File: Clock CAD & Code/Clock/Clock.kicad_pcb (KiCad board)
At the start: 2 copper layers, 140 x 90 mm, 64 parts, among them J1 Power_inlet_vertical, J2 Conn_01x06, SW1 RotaryEncoder_Switch, SW2 Omron_B3F_SPST, U1 L7805, U2 ATmega328-PU, U4 DS1307_DIP-8, U5 MAX7219, U6 MAX7219, Y1 Crystal 16MHZ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

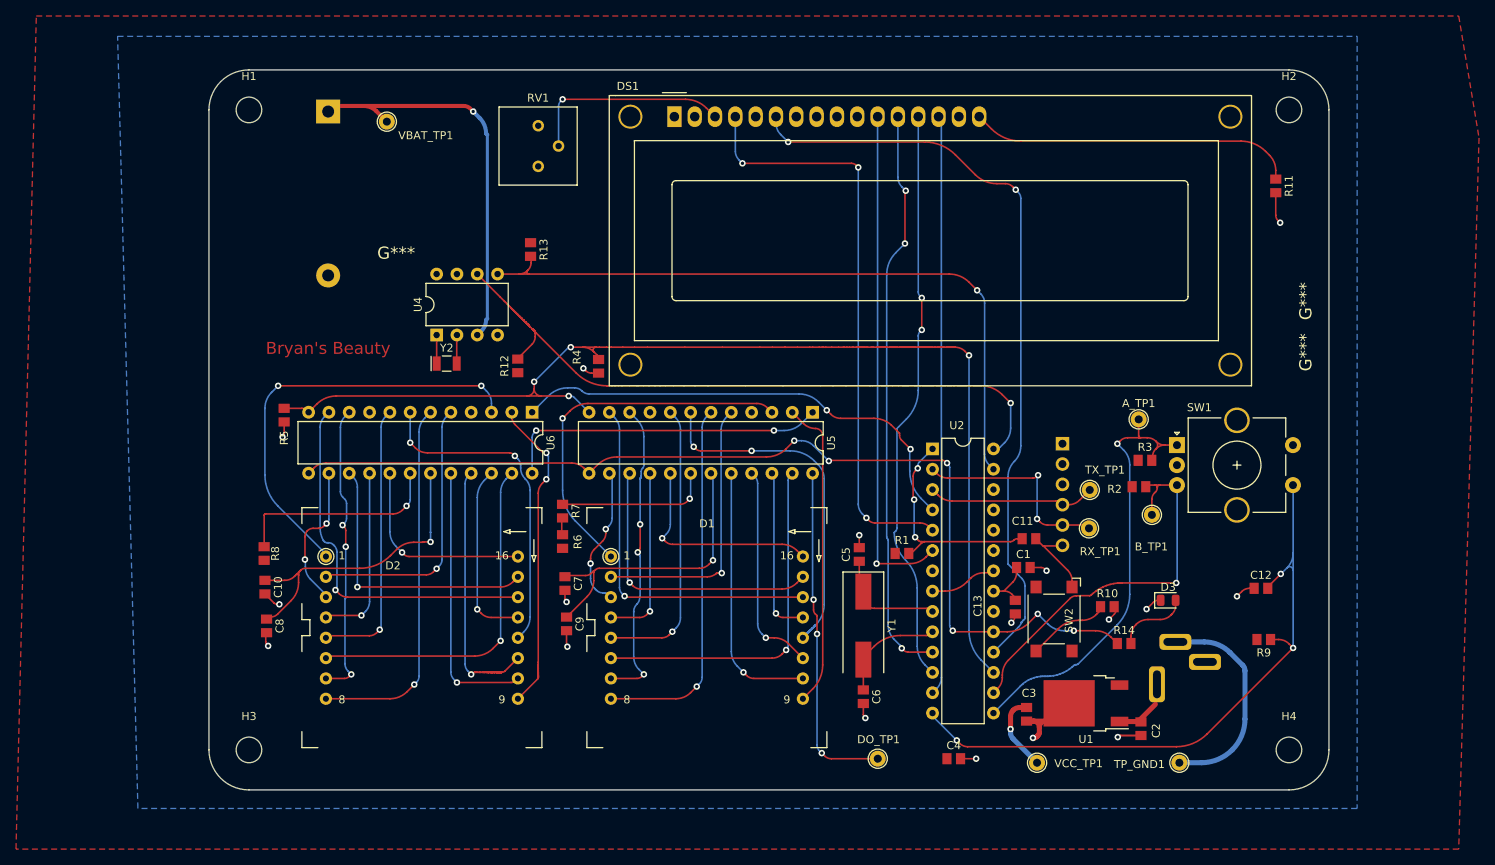
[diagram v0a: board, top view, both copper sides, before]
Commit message: Fixed DRC and ERC
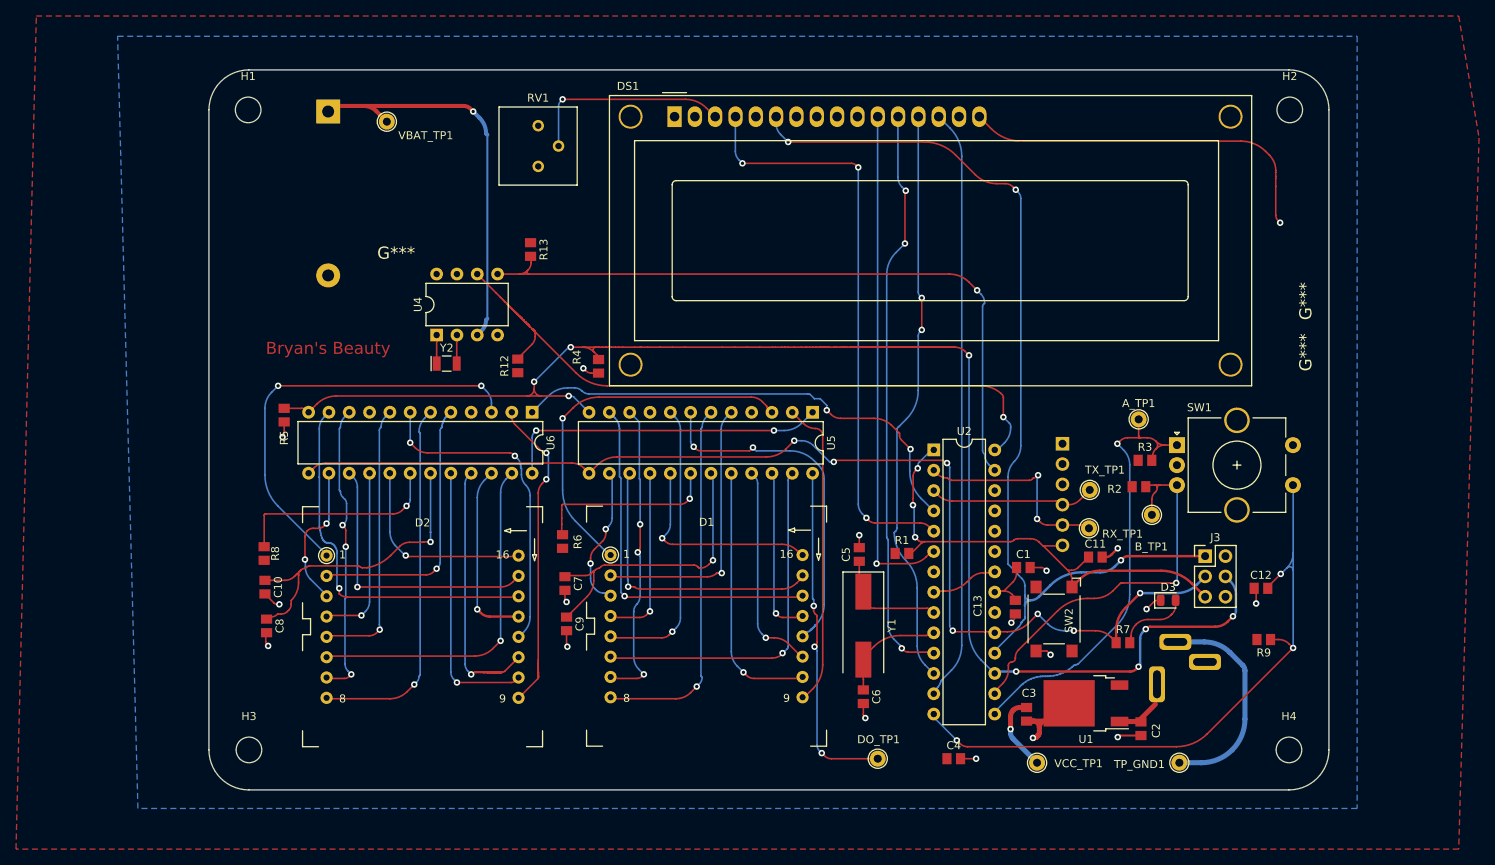
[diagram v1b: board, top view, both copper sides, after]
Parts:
- removed R10: R_0805_10K, footprints:R_0805_2012Metric
- removed R11, R14: R_0805_1K, footprints:R_0805_2012Metric
- added J3: Conn_02x03_Odd_Even, footprints:PinHeader_2x03_P2.54mm_Vertical, F.Cu at (204.5, 115.8)
- C11: value 100n -> C_0805_0.1uf
- R7: value R_0805_4.7K -> R_0805_2.2K
- moved R7 72.0 mm to (194.2, 126.6), turned to 0 degrees
- moved C11 8.61 mm to (190.8, 115.9)
- moved U2 0.20 mm to (170.6, 102.5)
- moved D1 0.19 mm to (142.2, 124.5)
- moved D2 0.14 mm to (106.7, 124.6)
- moved H1 0.10 mm to (84.9, 60.0)
- moved H2 0.10 mm to (215.1, 60.0)
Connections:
- net VBAT renamed Net-(BT1-Pad1)
- C11 pad 2: ~{RESET BTN} -> GND
- DS1 pad 16: Net-(DS1-Pad16) -> GND
- J2 pad 6: ~{RESET BTN} -> ~{RST}
- R4 pad 1: DATA MAX -> LOAD MAX
- R5 pad 1: DATA MAX -> LOAD MAX
- R7 pad 1: Net-(R6-Pad2) -> SCK
- R7 pad 2: Net-(R7-Pad2) -> Net-(D3-Pad2)
- SW2 pad 1: ~{RESET BTN} -> ~{RST}
- SW2 pad 4: Net-(SW2-Pad4) -> GND
- U2 pad 17: DATA MAX -> LOAD MAX
- U2 pad 4: LOAD MAX -> DATA MAX
- U5 pad 12: DATA MAX -> LOAD MAX
- U5 pad 18: Net-(R7-Pad2) -> Net-(R6-Pad2)
- U6 pad 1: LOAD MAX -> DATA MAX
- U6 pad 12: DATA MAX -> LOAD MAX
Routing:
- net LOAD MAX: track 59.9 -> 184.6 mm, vias 2 -> 8
- net DATA MAX: track 144.3 -> 60.5 mm, vias 4 -> 2
- net GND: track 80.1 -> 124.8 mm, vias 17 -> 18
- net Net-(DS1-Pad16): track 41.0 -> 0.00 mm
- net ~{RST}: track 28.5 -> 61.3 mm
- net LCD E: track 94.9 -> 120.6 mm, vias 2 -> 3
- net Net-(R6-Pad2): track 1.93 -> 23.2 mm, vias 0 -> 1
- net Net-(R7-Pad2): track 19.4 -> 0.00 mm, vias 1 -> 0
- net SCK: track 126.5 -> 142.7 mm, vias 6 -> 7
- net Net-(SW2-Pad4): track 10.3 -> 0.00 mm
- net ~{RESET BTN}: track 10.1 -> 0.00 mm
- net LCD D7: track 72.5 -> 74.2 mm
- net VCC: track 86.2 -> 87.1 mm
- net Net-(D1-Pad1): track 46.7 -> 47.3 mm
- net Net-(D1-Pad7): track 39.0 -> 38.4 mm
